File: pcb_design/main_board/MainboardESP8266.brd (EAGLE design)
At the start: 31 x 31 mm, 67 parts, among them U1 ATECC108-SSHDA

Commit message: Added IMU and temperature sensor to main board
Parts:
- removed R12: 15k, SparkFun-Resistors:0603-RES
- removed R7: 10K, SparkFun-Resistors:0603-RES
- added C10, C11, C9: 0.1uF, SparkFun-Capacitors:0603-CAP
- added C12: 10nF, SparkFun-Capacitors:0603-CAP
- added C15: 10uF, SparkFun-Capacitors:0603-CAP
- added D1, D2: (no value), SparkFun-LED:WS2812B
- added R18: 5k, SparkFun-Resistors:0603-RES@1
- added R19: (no value), SparkFun-Passives:0603-ARV
- added U2: TMP102, SparkFun-Sensors:SOT563
- added U3: LSM9DS1, LSM9DS1_temp:LGA24-8X4
- C1, C14, C2, C3, C4, C8: device SparkFun-Capacitors:0603-CAP -> SparkFun-Capacitors:0603-CAP@1
- R1, R13, R14, R15, R16, R17, R2, R3, R4, R5, R6, R9: device SparkFun-Resistors:0603-RES -> SparkFun-Resistors:0603-RES@1
- R10, R11: value 2.0k -> 4.7k
- moved JP6 25.6 mm to (28.0, 16.8)
- moved TP13 6.44 mm to (15.4, 5.60)
- moved TP14 3.86 mm to (1.90, 7.50)
- moved JP5 2.86 mm to (20.7, 1.10)
- moved TP12 2.02 mm to (13.3, 7.60)
- moved TP11 1.84 mm to (28.2, 4.80)
- moved JP4 0.50 mm to (9.00, 29.5)
- moved TP1 0.40 mm to (6.90, 29.5)
- moved U1 0.40 mm to (13.5, 15.1)
- flipped BTN_RST to the top, turned to 180 degrees
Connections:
- removed net GPIO16/STEPUP_EN: ESP8266.4, MCP1640.3, TP12.TP
- removed net GPIO4: ESP8266.14
- removed net N$4: ESP8266.6, R12.1, R7.1
- new net C1: C11.1, U3.24
- new net CAP: C12.1, U3.21
- new net CS_A/G: R19.2, U3.7
- new net CS_M: R19.1, U3.8
- new net DEN_A/G: U3.13
- new net DRDY_M: U3.9
- new net GPIO16/RGB: D1.4, ESP8266.4
- new net GPIO4/STEPUP_EN: ESP8266.14, MCP1640.3, TP12.TP
- new net INT1_A/G: U3.11
- new net INT2_A/G: U3.12
- new net INT_M: U3.10
- new net L1OUT: D1.2, D2.4
- new net L2OUT: D2.2
- new net N$10: R18.2, U2.3
- new net RESET_AT: ESP8266.6, JP_RST.1
- new net SDO_A/G: R19.4, U3.5
- new net SDO_M: R19.3, U3.6
- net GND: now also C10.2, C11.2, C12.2, C15.2, C9.2, D1.3, D2.3, U2.2, U2.4, U3.14, U3.15, U3.16, U3.17, U3.18, U3.19, U3.20; no longer R12.2
- net GPIO14/SCL: now also U2.1, U3.2
- net GPIO2/SDA: now also U2.6, U3.4
- net STAT: no longer R7.2
- net VCC: now also C10.1, C15.1, C9.1, D1.1, D2.1, R18.1, R19.5, R19.6, R19.7, R19.8, U2.5, U3.1, U3.22, U3.23, U3.3
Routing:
- net VCC: track 80.1 -> 127.9 mm
- net RESET_AT: track 0.00 -> 36.3 mm, vias 0 -> 3
- net GPIO4/STEPUP_EN: track 0.00 -> 28.5 mm, vias 0 -> 3
- net GPIO14/SCL: track 41.0 -> 59.7 mm, vias 3 -> 5
- net GND: track 14.8 -> 29.4 mm, vias 7 -> 11
- net GPIO16/RGB: track 0.00 -> 14.0 mm, vias 0 -> 2
- net L1OUT: track 0.00 -> 11.9 mm, vias 0 -> 2
- net GPIO2/SDA: track 28.9 -> 40.0 mm
- net GPIO16/STEPUP_EN: track 9.37 -> 0.00 mm, vias 1 -> 0
- net STAT: track 8.97 -> 1.64 mm
- net N$4: track 5.03 -> 0.00 mm, vias 1 -> 0
- net CS_M: track 0.00 -> 3.93 mm
- net SDO_A/G: track 0.00 -> 3.50 mm
- net CS_A/G: track 0.00 -> 3.48 mm
- net VSWITCH: track 43.2 -> 39.8 mm
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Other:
- board text added: "20102016"
- board text added: "RST AT"
- board text added: "U1"
- board text added: "U2"
- board text removed: "08092016"
- board text removed: "GRITSBot"

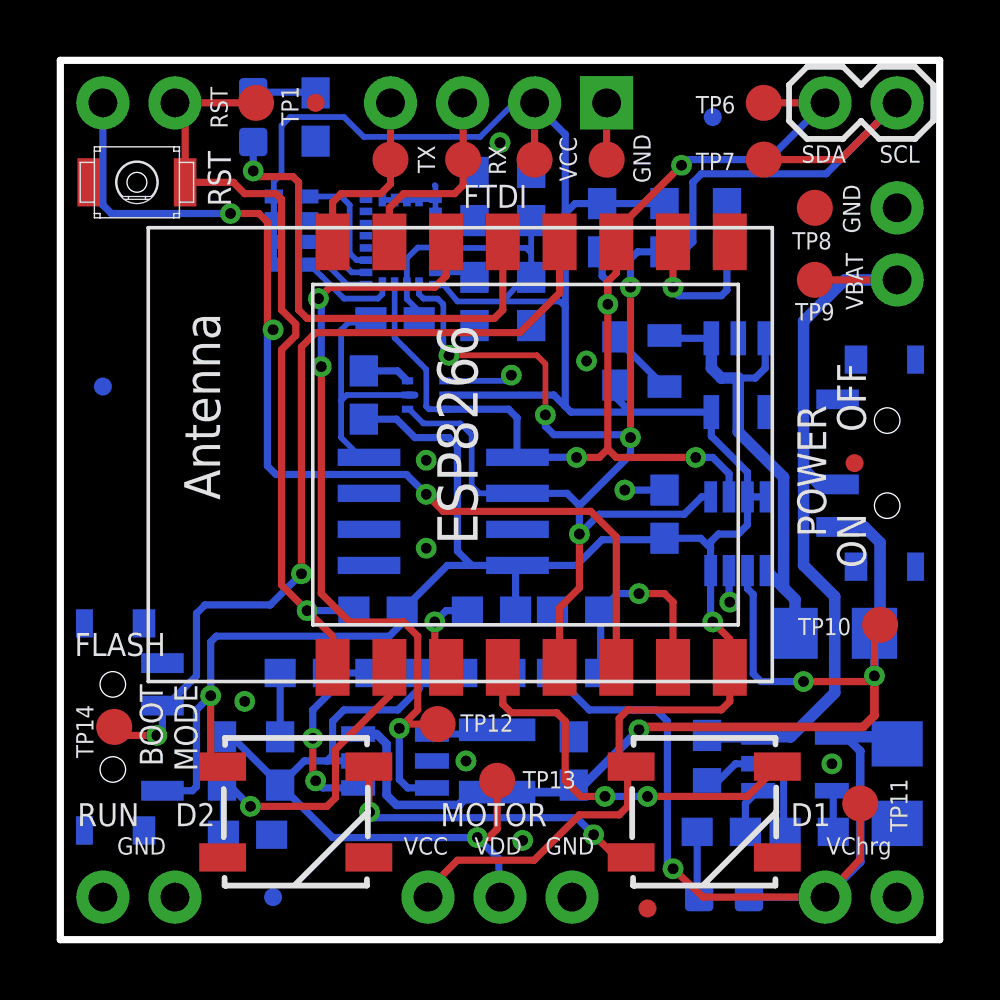
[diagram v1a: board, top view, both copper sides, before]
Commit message: Fixed RGB LED setup on main board.
The RGB LEDs were connected to GPIO16, which on some versions
of the ESP8266 is connected to the RESET pin and can't be used
as general purpose pin after all. The RGB LEDs are now connected
to GPIO5 - the same pin as the status LED. Both types of LEDs can
be used together on the same pin.
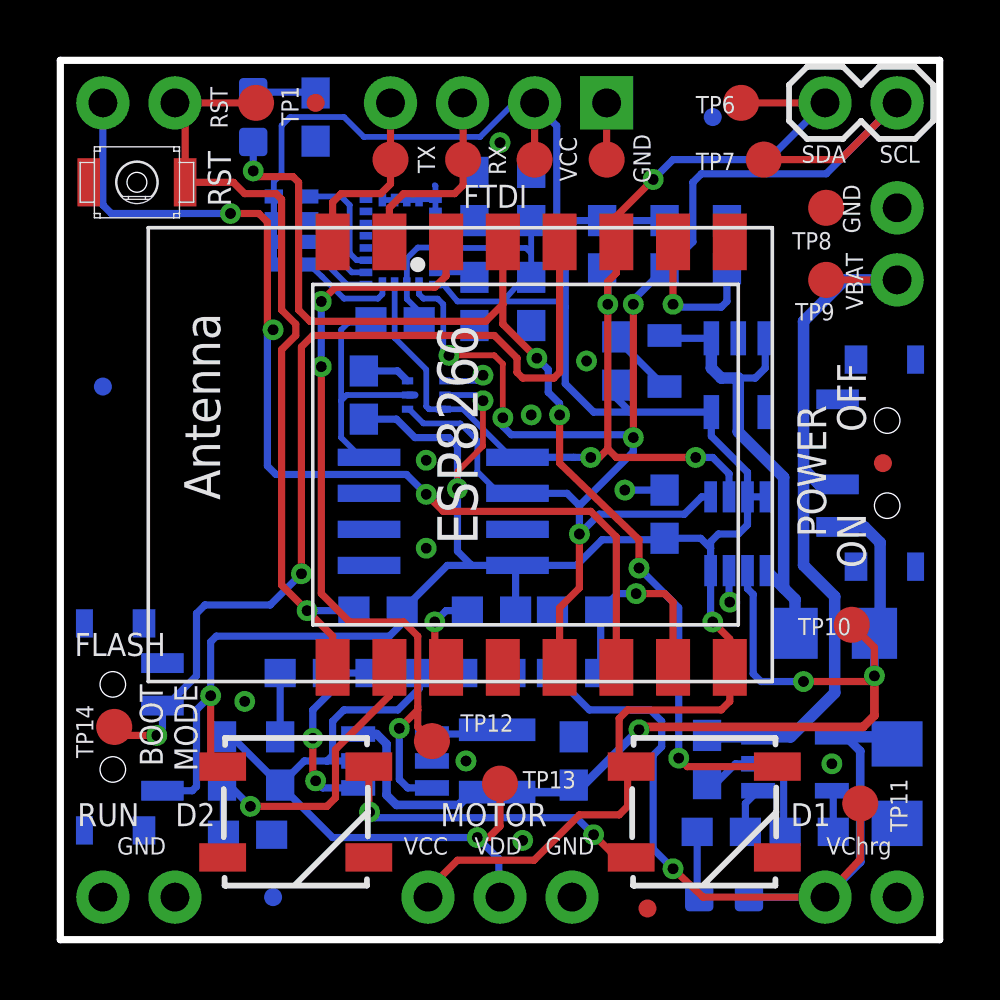
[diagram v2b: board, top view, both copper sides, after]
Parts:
- R19: value (none) -> 10k
- moved JP6 1.00 mm to (29.0, 16.8)
- moved TP10 1.00 mm to (27.9, 11.1)
- moved TP6 0.80 mm to (24.0, 29.5)
- moved TP12 0.63 mm to (13.1, 7.00)
- moved R1 0.60 mm to (23.5, 24.5)
- moved R10 0.60 mm to (19.1, 24.5)
- moved R11 0.60 mm to (21.3, 24.5)
- moved TP8 0.40 mm to (27.0, 25.8)
- moved TP9 0.40 mm to (27.0, 23.3)
- moved TP13 0.14 mm to (15.5, 5.50)
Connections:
- removed net GPIO16/RGB: D1.4, ESP8266.4
- removed net GPIO5: ESP8266.13, LED_USER.A
- new net GPIO5_LEDS: D1.4, ESP8266.13, LED_USER.A
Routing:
- net GPIO5_LEDS: track 0.00 -> 39.7 mm, vias 0 -> 5
- net GPIO5: track 17.4 -> 0.00 mm, vias 1 -> 0
- net GPIO16/RGB: track 14.0 -> 0.00 mm, vias 2 -> 0
- net GPIO0: track 30.6 -> 33.7 mm
- net GPIO14/SCL: track 59.7 -> 58.5 mm
- net GND: track 29.4 -> 28.4 mm, vias 11 -> 12
- net VCC: track 127.9 -> 128.0 mm, vias 2 -> 4

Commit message: Moved test pads to account for pogo pin holes on tester boards
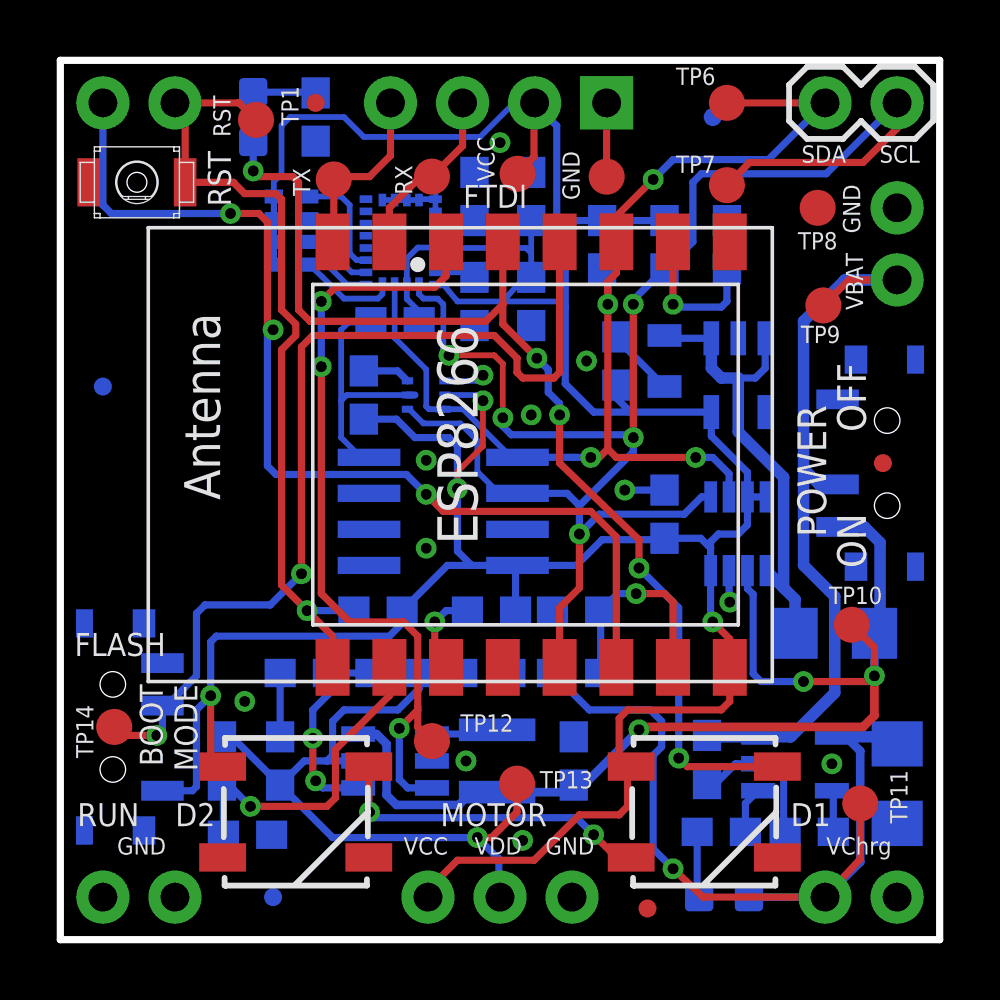
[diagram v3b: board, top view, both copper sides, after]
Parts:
- moved TP2 2.12 mm to (9.64, 26.8)
- moved TP7 1.58 mm to (23.5, 26.6)
- moved TP3 1.25 mm to (13.1, 26.9)
- moved TP9 0.91 mm to (26.9, 22.4)
- moved TP4 0.78 mm to (16.1, 27.0)
- moved TP1 0.60 mm to (6.90, 28.9)
- moved TP13 0.60 mm to (16.1, 5.50)
- moved TP5 0.60 mm to (19.3, 26.9)
- moved TP6 0.50 mm to (23.5, 29.5)
- moved TP8 0.30 mm to (26.7, 25.8)
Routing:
- net GPIO14/SCL: track 58.5 -> 60.7 mm
- net U0RXI: track 7.04 -> 6.23 mm
- net VCC: track 128.0 -> 128.7 mm
- net GND: track 28.4 -> 29.0 mm
- net GPIO2/SDA: track 39.9 -> 40.4 mm

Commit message: Added test pin for GPIO5
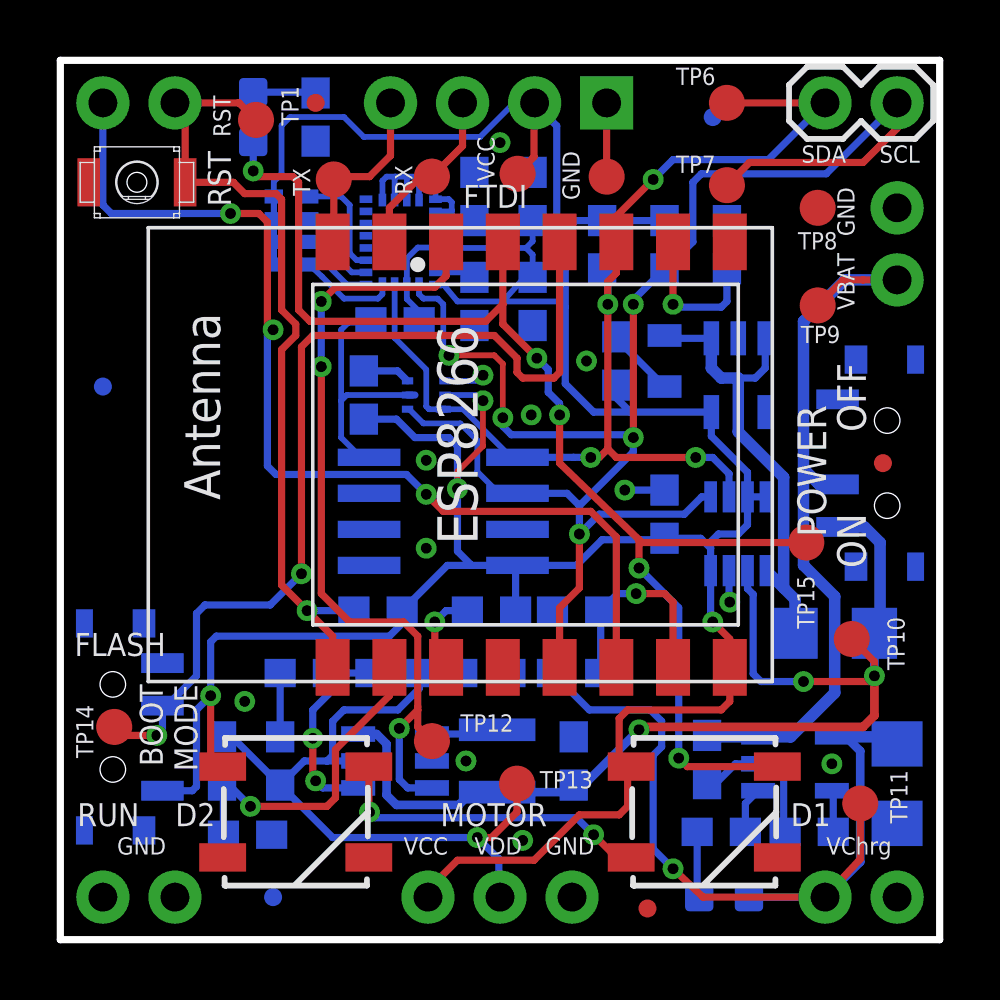
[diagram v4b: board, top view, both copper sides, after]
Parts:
- added TP15: PTR1B1,27, testpad:B1,27
- moved TP10 0.50 mm to (27.9, 10.6)
- moved TP9 0.20 mm to (26.7, 22.4)
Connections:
- net GPIO5_LEDS: now also TP15.TP
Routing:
- net GPIO5_LEDS: track 39.7 -> 45.6 mm
- net GND: track 29.0 -> 34.1 mm
- net VCC: track 128.7 -> 129.3 mm
- net VSWITCH: track 40.0 -> 39.5 mm
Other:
- board text added: "09112016"
- board text added: "v8.0"
- board text removed: "20102016"
- board text removed: "v7.0"
